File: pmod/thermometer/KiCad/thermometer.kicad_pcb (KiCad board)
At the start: 2 copper layers, 23 x 17 mm, 4 parts, among them J1 Conn_01x06_Pin, U1 DS18B20

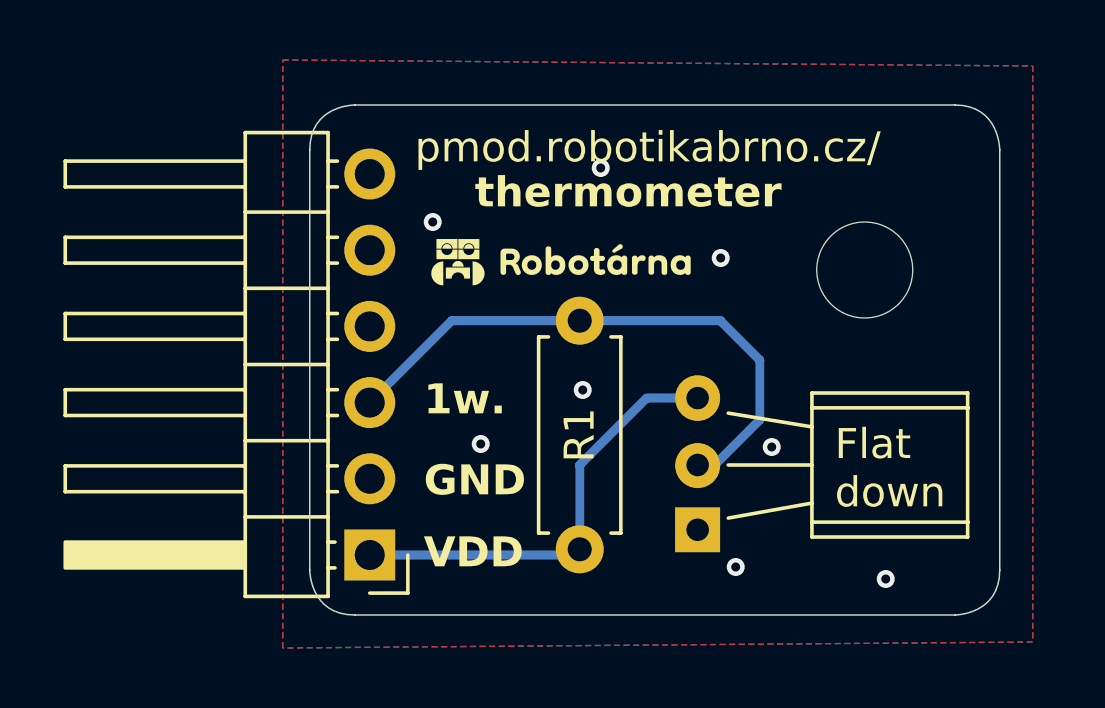
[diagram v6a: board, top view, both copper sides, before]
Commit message: fix: prepare all board for manufacturing
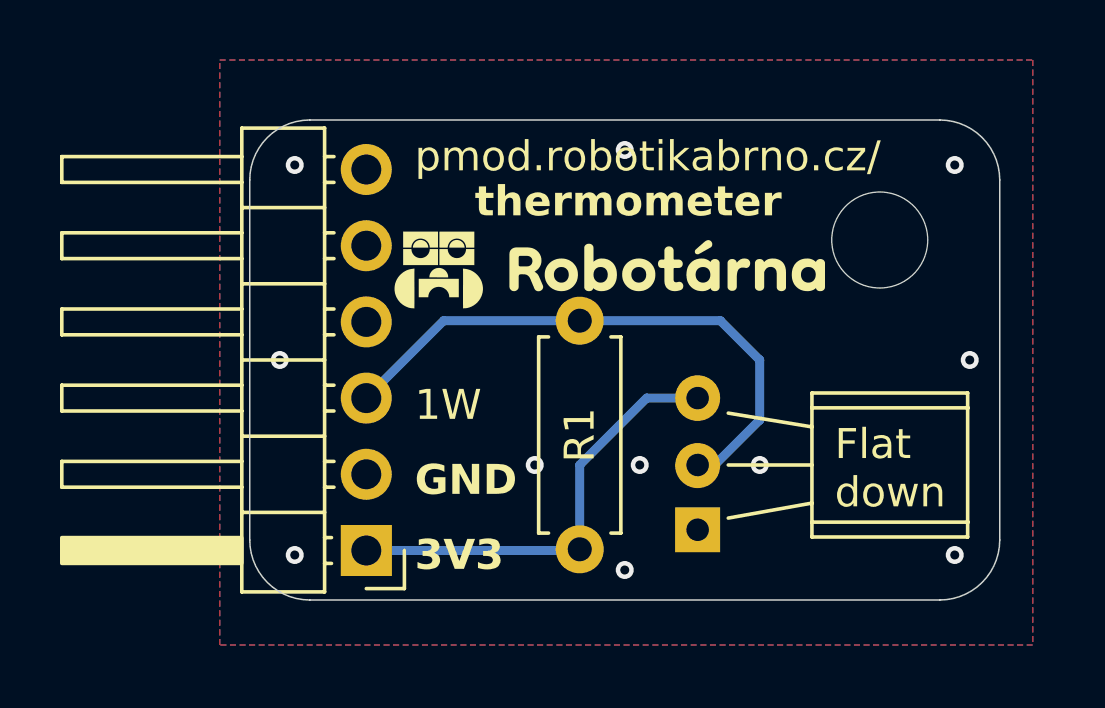
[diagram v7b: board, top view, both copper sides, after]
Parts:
- moved H1 1.12 mm to (157.5, 106.0)
- moved J1 0.19 mm to (140.4, 116.3)
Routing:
- net GND: vias 8 -> 11
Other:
- board size 23 x 17 mm -> 25 x 16 mm
- board text added: "1W"
- board text added: "36mm"
- board text added: "3V3"
- board text added: "50mm"
- board text removed: "1w."
- board text removed: "VDD"

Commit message: fix: thermometer silkscreen dimensions & voltage
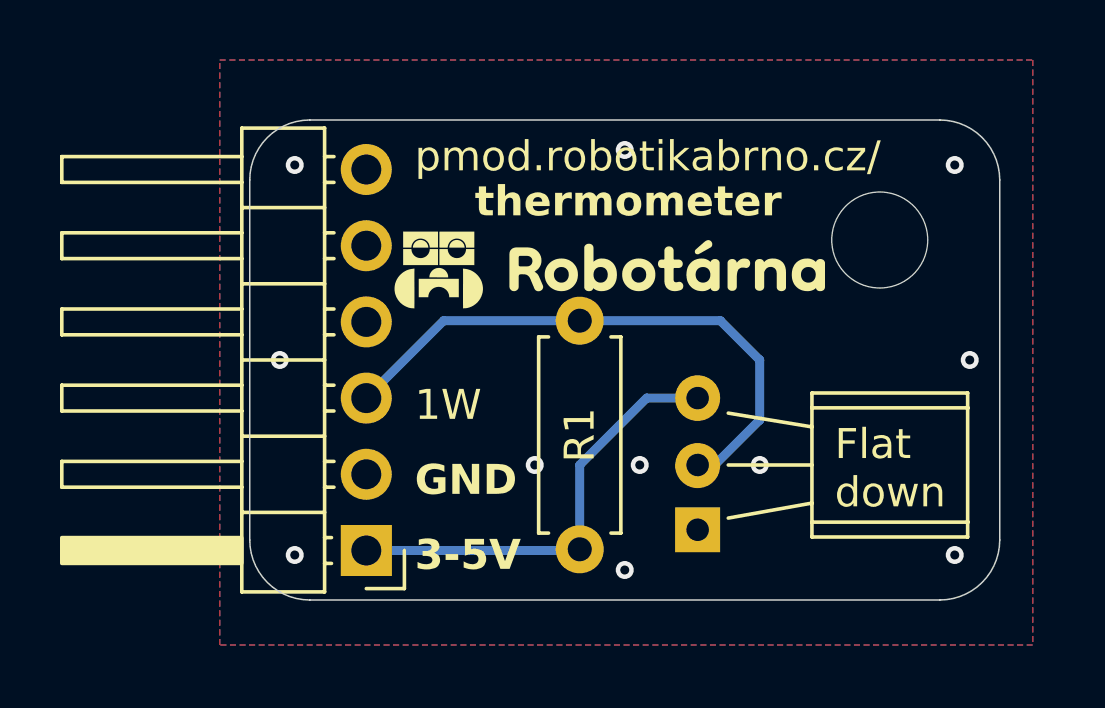
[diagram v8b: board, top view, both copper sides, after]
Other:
- board text added: "16mm"
- board text added: "25mm"
- board text added: "3-5V"
- board text removed: "36mm"
- board text removed: "3V3"
- board text removed: "50mm"
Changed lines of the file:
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@@
 		)
 	)
-	(gr_text "3V3"
+	(gr_text "3-5V"
 		(at 142 116.5 0)
 		(layer "F.SilkS")
@@
 		)
 	)
-	(gr_text "36mm"
-		(at 146.5 110.75 -0)
+	(gr_text "16mm"
+		(at 146.5 110.75 0)
 		(layer "B.SilkS")
 		(effects
@@
 		)
 	)
-	(gr_text "50mm"
-		(at 148.5 114.75 -0)
+	(gr_text "25mm"
+		(at 148.5 114.75 0)
 		(layer "B.SilkS")
 		(effects
